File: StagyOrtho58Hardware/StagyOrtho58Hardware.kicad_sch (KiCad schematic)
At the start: 30 parts

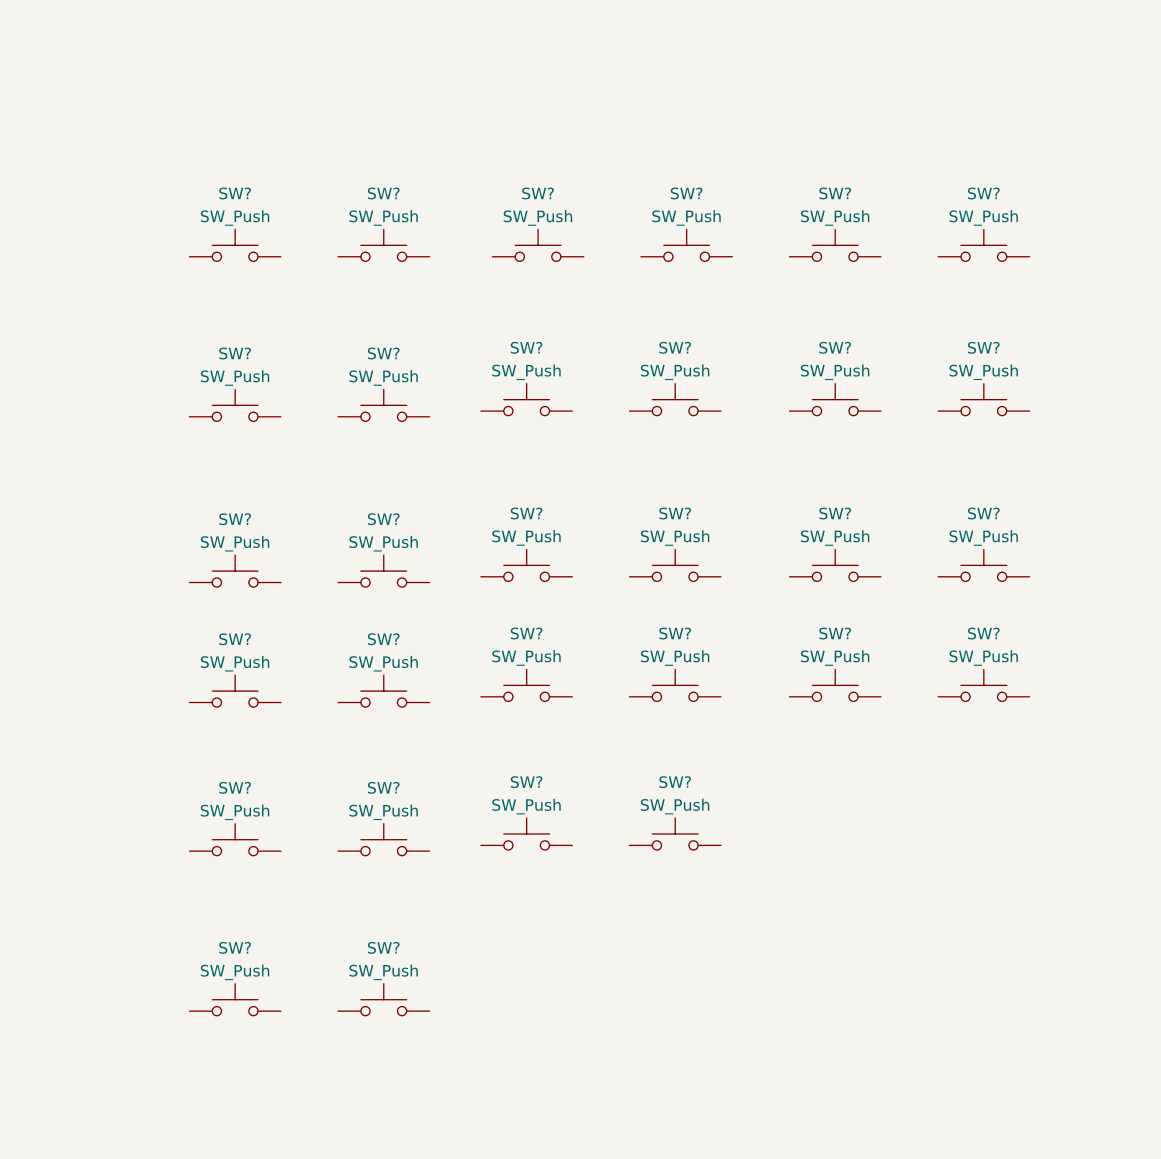
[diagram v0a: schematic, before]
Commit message: Key switches matrix 6x5 with diodes
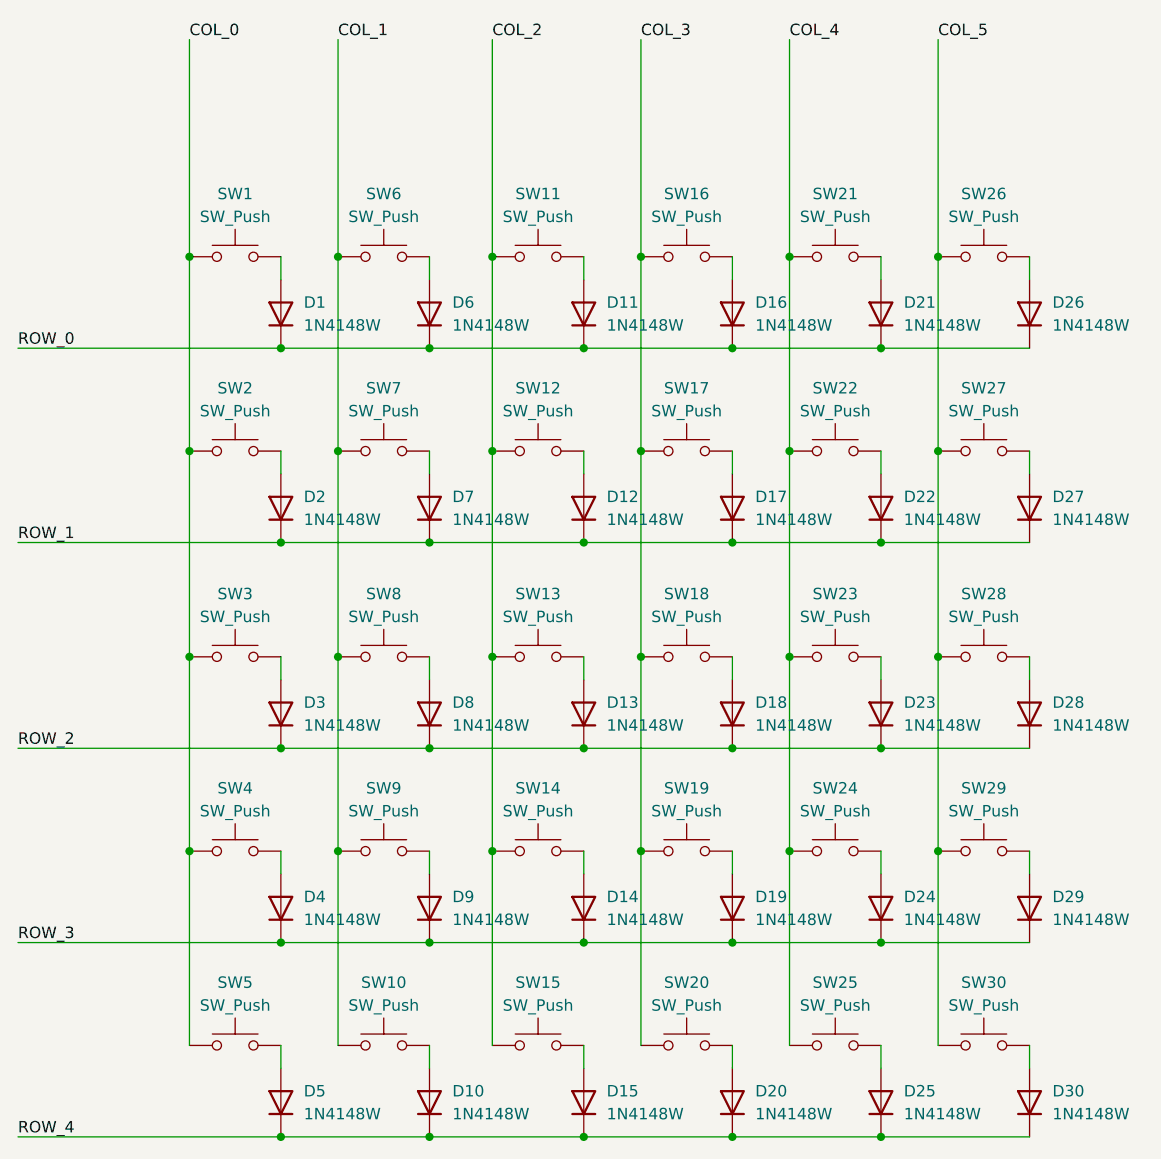
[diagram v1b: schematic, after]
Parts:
- removed SW? (x24): SW_Push, symbol Switch:SW_Push
- added D1, D10, D11, D12, D13, D14, D15, D16, D17, D18, D19, D2, D20, D21, D22, D23, D24, D25, D26, D27, D28, D29, D3, D30, D4, D5, D6, D7, D8, D9: 1N4148W, Diode_SMD:D_SOD-123, symbol Diode:1N4148W
- added SW10, SW12, SW13, SW14, SW15, SW17, SW18, SW19, SW2, SW20, SW22, SW23, SW24, SW25, SW27, SW28, SW29, SW3, SW30, SW4, SW5, SW7, SW8, SW9: SW_Push, symbol Switch:SW_Push
- gave numbers to parts that had none: 6
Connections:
- net COL_2: now reaches SW11.1
- net COL_2: now also SW12.1, SW13.1, SW14.1, SW15.1
- net at SW11.2: now also D11.2 (A)
- net COL_0: now reaches SW1.1
- net COL_0: now also SW2.1, SW3.1, SW4.1, SW5.1
- net at SW1.2: now also D1.2 (A)
- net COL_5: now reaches SW26.1
- net COL_5: now also SW27.1, SW28.1, SW29.1, SW30.1
- net at SW26.2: now also D26.2 (A)
- net COL_1: now reaches SW6.1
- net COL_1: now also SW10.1, SW7.1, SW8.1, SW9.1
- net at SW6.2: now also D6.2 (A)
- net COL_4: now reaches SW21.1
- net COL_4: now also SW22.1, SW23.1, SW24.1, SW25.1
- net at SW21.2: now also D21.2 (A)
- net COL_3: now reaches SW16.1
- net COL_3: now also SW17.1, SW18.1, SW19.1, SW20.1
- net at SW16.2: now also D16.2 (A)
- new net: D15.2 (A), SW15.2
- new net: D4.2 (A), SW4.2
- new net: D29.2 (A), SW29.2
- new net: D30.2 (A), SW30.2
- new net: D28.2 (A), SW28.2
- new net: D2.2 (A), SW2.2
- new net: D3.2 (A), SW3.2
- new net: D20.2 (A), SW20.2
- new net: D9.2 (A), SW9.2
- new net: D22.2 (A), SW22.2
- new net: D13.2 (A), SW13.2
- new net: D27.2 (A), SW27.2
- new net: D18.2 (A), SW18.2
- new net: D24.2 (A), SW24.2
- new net: D12.2 (A), SW12.2
- new net: D5.2 (A), SW5.2
- new net: D25.2 (A), SW25.2
- new net: D17.2 (A), SW17.2
- new net: D10.2 (A), SW10.2
- new net: D23.2 (A), SW23.2
- new net: D8.2 (A), SW8.2
- new net: D7.2 (A), SW7.2
- new net: D19.2 (A), SW19.2
- new net: D14.2 (A), SW14.2
- new net ROW_0: D1.1 (K), D11.1 (K), D16.1 (K), D21.1 (K), D26.1 (K), D6.1 (K)
- new net ROW_1: D12.1 (K), D17.1 (K), D2.1 (K), D22.1 (K), D27.1 (K), D7.1 (K)
- new net ROW_2: D13.1 (K), D18.1 (K), D23.1 (K), D28.1 (K), D3.1 (K), D8.1 (K)
- new net ROW_3: D14.1 (K), D19.1 (K), D24.1 (K), D29.1 (K), D4.1 (K), D9.1 (K)
- new net ROW_4: D10.1 (K), D15.1 (K), D20.1 (K), D25.1 (K), D30.1 (K), D5.1 (K)

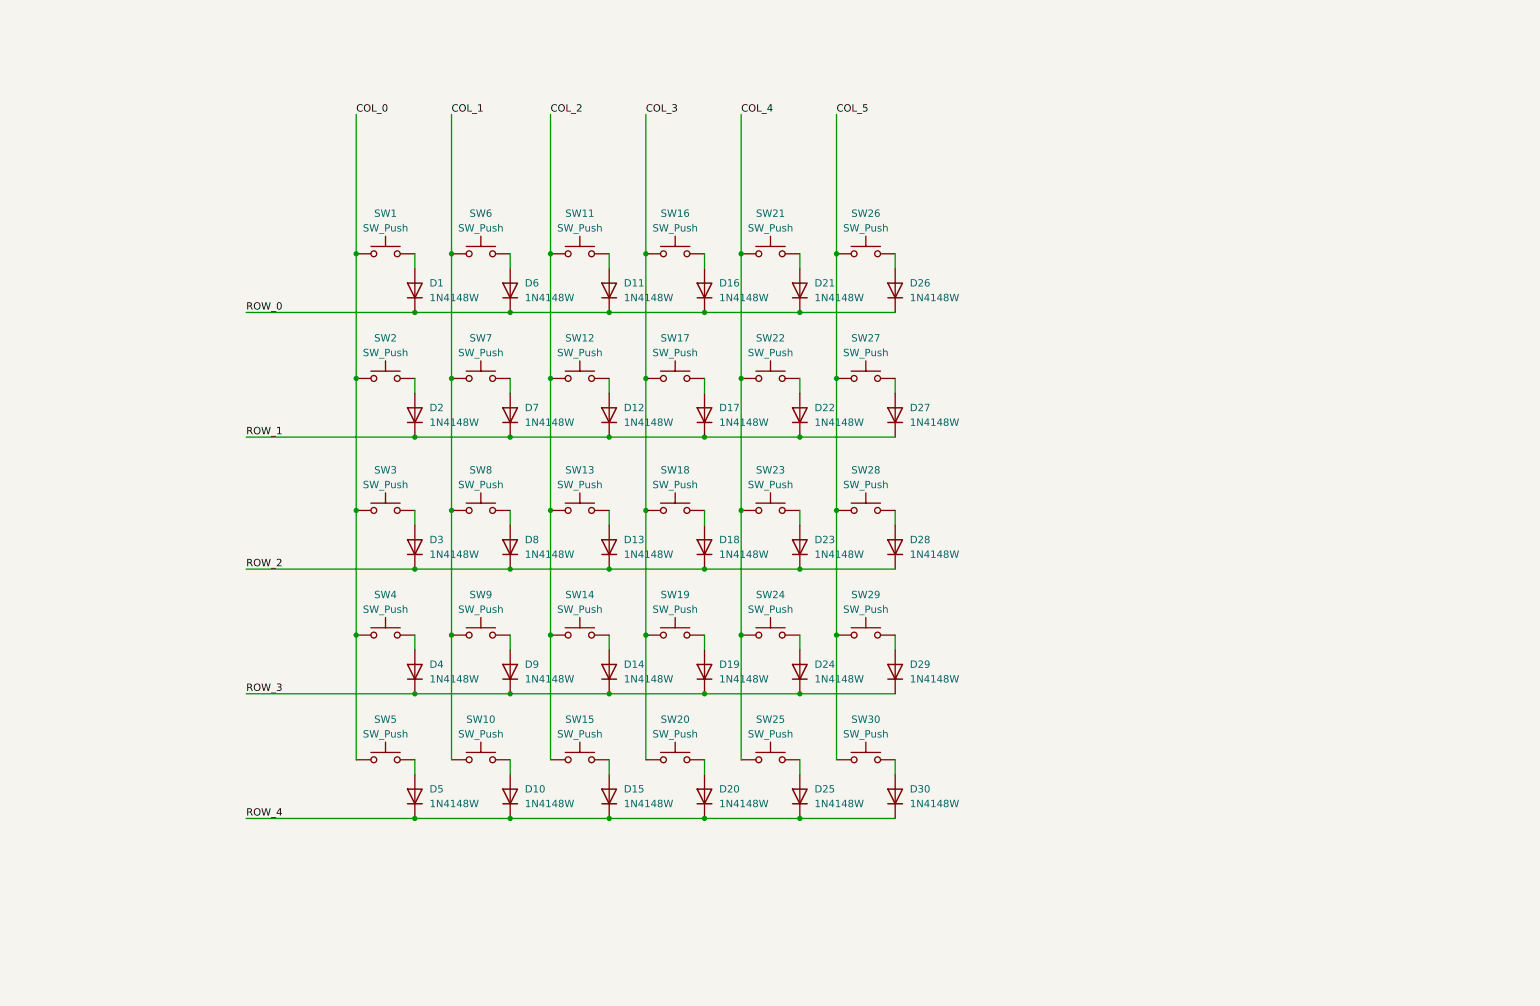
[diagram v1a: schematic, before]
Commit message: Adds ports expander and USB-C for split bridge
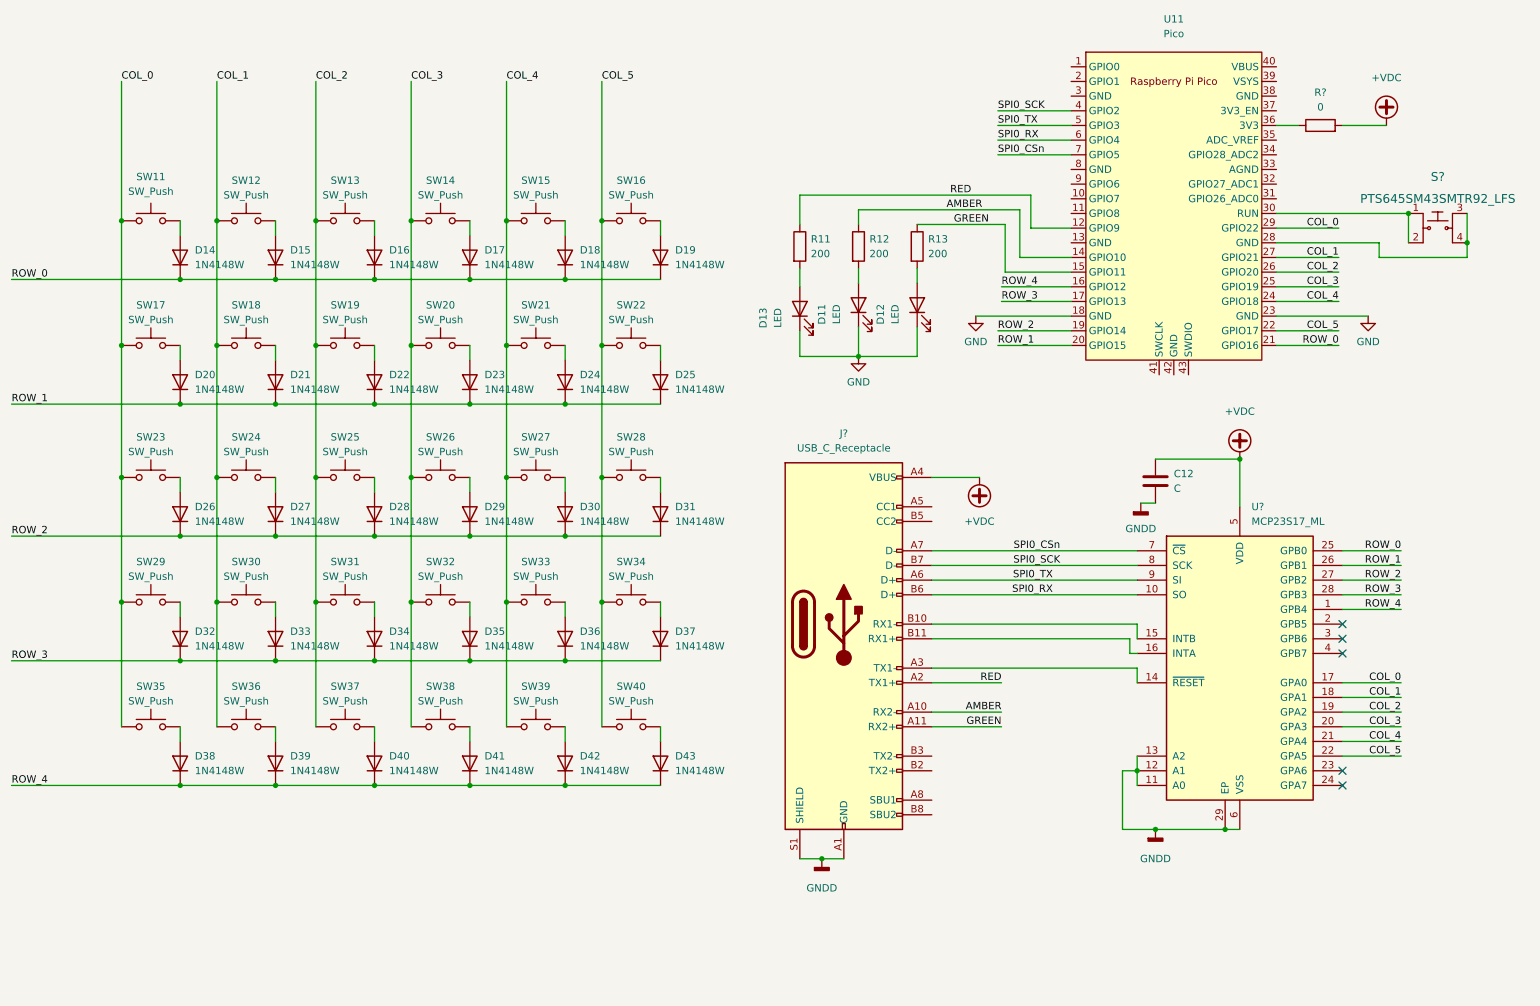
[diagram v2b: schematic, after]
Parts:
- added C12: C, Capacitor_SMD:C_0603_1608Metric, symbol Device:C
- added D11, D12, D13: LED, LED_SMD:LED_0603_1608Metric_Pad1.05x0.95mm_HandSolder, symbol Device:LED
- added J?: USB_C_Receptacle, symbol Connector:USB_C_Receptacle
- added R11, R12, R13: 200, Resistor_SMD:R_0603_1608Metric_Pad0.98x0.95mm_HandSolder, symbol Device:R
- added R?: 0, Resistor_SMD:R_0603_1608Metric_Pad0.98x0.95mm_HandSolder, symbol Device:R
- added S?: PTS645SM43SMTR92_LFS, digikey-footprints:Switch_Tactile_SMD_6x6mm_PTS645, symbol dk_Tactile-Switches:PTS645SM43SMTR92_LFS
- added U11: Pico, MCU_RaspberryPi_and_Boards:RPi_Pico_SMD_TH, symbol MCU_RaspberryPi_and_Boards:Pico
- added U?: MCP23S17_ML, Package_DFN_QFN:QFN-28-1EP_6x6mm_P0.65mm_EP4.25x4.25mm, symbol Interface_Expansion:MCP23S17_ML
- renumbered D1 to D14, D6 to D15, D11 to D16, D16 to D17, D21 to D18, D26 to D19, D2 to D20, D7 to D21, D12 to D22, D17 to D23, D22 to D24, D27 to D25, D3 to D26, D8 to D27, D13 to D28, D18 to D29, D23 to D30, D28 to D31, D4 to D32, D9 to D33, D14 to D34, D19 to D35, D24 to D36, D29 to D37, D5 to D38, D10 to D39, D15 to D40, D20 to D41, D25 to D42, D30 to D43, SW1 to SW11, SW6 to SW12, SW11 to SW13, SW16 to SW14, SW21 to SW15, SW26 to SW16, SW2 to SW17, SW7 to SW18, SW12 to SW19, SW17 to SW20, SW22 to SW21, SW27 to SW22, SW3 to SW23, SW8 to SW24, SW13 to SW25, SW18 to SW26, SW23 to SW27, SW4 to SW29, SW9 to SW30, SW14 to SW31, SW19 to SW32, SW24 to SW33, SW29 to SW34, SW5 to SW35, SW10 to SW36, SW15 to SW37, SW20 to SW38, SW25 to SW39, SW30 to SW40
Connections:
- net COL_0: now also U11.29 (GPIO22), U?.17 (GPA0)
- net COL_1: now also U11.27 (GPIO21), U?.18 (GPA1)
- net COL_2: now also U11.26 (GPIO20), U?.19 (GPA2)
- net COL_3: now also U11.25 (GPIO19), U?.20 (GPA3)
- net COL_4: now also U11.24 (GPIO18), U?.21 (GPA4)
- net COL_5: now also U11.22 (GPIO17), U?.22 (GPA5)
- net ROW_0: now also U11.21 (GPIO16), U?.25 (GPB0)
- net ROW_1: now also U11.20 (GPIO15), U?.26 (GPB1)
- net ROW_2: now also U11.19 (GPIO14), U?.27 (GPB2)
- net ROW_3: now also U11.17 (GPIO13), U?.28 (GPB3)
- net ROW_4: now also U11.16 (GPIO12), U?.1 (GPB4)
- new net: D13.2 (A), R11.2
- new net: D11.2 (A), R12.2
- new net: R?.1, U11.36 (3V3)
- new net: D12.2 (A), R13.2
- new net: S?.3, S?.4, U11.28 (GND)
- new net: S?.1, S?.2, U11.30 (RUN)
- new net: J?.A3 (TX1-), U?.14 (~{RESET})
- new net: J?.B10 (RX1-), U?.15 (INTB)
- new net: J?.B11 (RX1+), U?.16 (INTA)
- new net +VDC: C12.1, J?.A4 (VBUS), J?.A9 (VBUS), J?.B4 (VBUS), J?.B9 (VBUS), R?.2, U?.5 (VDD)
- new net AMBER: J?.A10 (RX2-), R12.1, U11.14 (GPIO10)
- new net GND: D11.1 (K), D12.1 (K), D13.1 (K), U11.18 (GND), U11.23 (GND)
- new net GNDD: C12.2, J?.A1 (GND), J?.A12 (GND), J?.B1 (GND), J?.B12 (GND), J?.S1 (SHIELD), U?.11 (A0), U?.12 (A1), U?.13 (A2), U?.29 (EP), U?.6 (VSS)
- new net GREEN: J?.A11 (RX2+), R13.1, U11.15 (GPIO11)
- new net RED: J?.A2 (TX1+), R11.1, U11.12 (GPIO9)
- new net SPI0_CSn: J?.A7 (D-), U11.7 (GPIO5), U?.7 (~{CS})
- new net SPI0_RX: J?.B6 (D+), U11.6 (GPIO4), U?.10 (SO)
- new net SPI0_SCK: J?.B7 (D-), U11.4 (GPIO2), U?.8 (SCK)
- new net SPI0_TX: J?.A6 (D+), U11.5 (GPIO3), U?.9 (SI)
- no-connect marks 0 -> 5
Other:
- company: (none) -> 125 Systems
- title: (none) -> Staggered Ortholinear (29 +1) x 2 Keys Split Keyboard
- moved on the sheet: D14, D15, D16, D17, D18, D19, D20, D21, D22, D23, D24, D25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

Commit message: Assigns inner 4x4 switches 1u footprints
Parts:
- SW12, SW13, SW14, SW15, SW16, SW18, SW19, SW20, SW21, SW22, SW24, SW25, SW26, SW27, SW28, SW30, SW31, SW32, SW33, SW34: footprint (none) -> Switch_Keyboard_Kailh:SW_Kailh_Choc_V1V2_1.00u
- gave numbers to parts that had none: 4

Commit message: Assigns Ctrl, Cmd, Alt switches 1.25u footprints
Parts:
- SW35, SW36, SW37: footprint (none) -> Switch_Keyboard_Kailh:SW_Kailh_Choc_V1V2_1.25u
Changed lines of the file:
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@@
     (property "Reference" "SW35" (id 0) (at 46.99 135.255 0))
     (property "Value" "SW_Push" (id 1) (at 46.99 137.795 0))
-    (property "Footprint" "" (id 2) (at 46.99 137.16 0)
+    (property "Footprint" "Switch_Keyboard_Kailh:SW_Kailh_Choc_V1V2_1.25u" (id 2) (at 46.99 137.16 0)
       (effects (font (size 1.27 1.27)) hide)
     )
@@
     (property "Reference" "SW36" (id 0) (at 63.5 135.255 0))
     (property "Value" "SW_Push" (id 1) (at 63.5 137.795 0))
-    (property "Footprint" "" (id 2) (at 63.5 137.16 0)
+    (property "Footprint" "Switch_Keyboard_Kailh:SW_Kailh_Choc_V1V2_1.25u" (id 2) (at 63.5 137.16 0)
       (effects (font (size 1.27 1.27)) hide)
     )
@@
     (property "Reference" "SW37" (id 0) (at 80.645 135.255 0))
     (property "Value" "SW_Push" (id 1) (at 80.645 137.795 0))
-    (property "Footprint" "" (id 2) (at 80.645 137.16 0)
+    (property "Footprint" "Switch_Keyboard_Kailh:SW_Kailh_Choc_V1V2_1.25u" (id 2) (at 80.645 137.16 0)
       (effects (font (size 1.27 1.27)) hide)
     )
@@
     )
     (path "/b61c3e02-78ec-4875-b5a7-fba1468acaf9"
-      (reference "SW35") (unit 1) (value "SW_Push") (footprint "")
+      (reference "SW35") (unit 1) (value "SW_Push") (footprint "Switch_Keyboard_Kailh:SW_Kailh_Choc_V1V2_1.25u")
     )
     (path "/e2d13c09-bfa4-4a1c-bb32-a1d753622985"
-      (reference "SW36") (unit 1) (value "SW_Push") (footprint "")
+      (reference "SW36") (unit 1) (value "SW_Push") (footprint "Switch_Keyboard_Kailh:SW_Kailh_Choc_V1V2_1.25u")
     )
     (path "/f3f81d51-470c-4e92-9834-6924230cef2e"
-      (reference "SW37") (unit 1) (value "SW_Push") (footprint "")
+      (reference "SW37") (unit 1) (value "SW_Push") (footprint "Switch_Keyboard_Kailh:SW_Kailh_Choc_V1V2_1.25u")
     )
     (path "/3d1dea62-0eee-4a9a-93fb-3c3995e9536a"
